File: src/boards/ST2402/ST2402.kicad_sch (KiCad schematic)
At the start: 21 parts, among them J1 Conn_02x19_Odd_Even, J2 Conn_02x19_Odd_Even, J3 Conn_01x08, J4 Conn_01x08, J5 Conn_01x06, J6 Conn_01x10, J7 Conn_01x02, J8 Conn_01x02

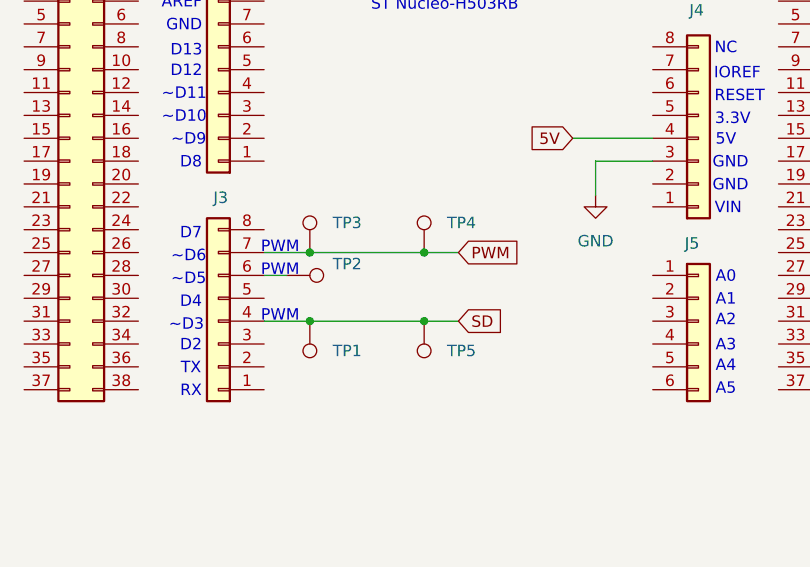
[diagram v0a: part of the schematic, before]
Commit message: Updated pcb files
Added r2 and r3 gerbers and updated KiCad file (r3)
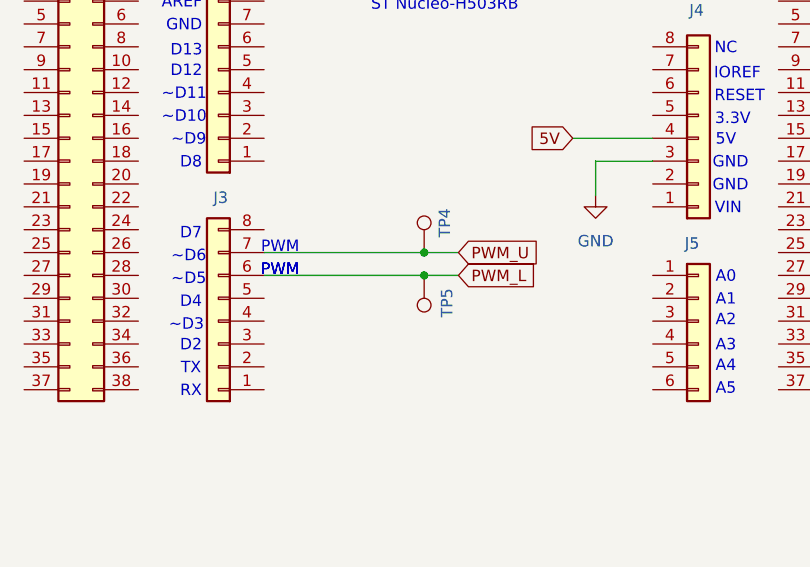
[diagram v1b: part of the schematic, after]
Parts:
- removed TP1, TP2, TP3: TestPoint, TestPoint:TestPoint_THTPad_D2.0mm_Drill1.0mm, symbol Connector:TestPoint
- TP4, TP5: footprint TestPoint:TestPoint_THTPad_D2.0mm_Drill1.0mm -> TestPoint:TestPoint_Keystone_5010-5014_Multipurpose
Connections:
- net PWM_L: now reaches J3.6 (Pin_6)
- net PWM_L: now also TP5.1
- net PWM renamed PWM_U
- net SD: no longer names the net of J3.4 (Pin_4)
- net SD: no longer TP5.1
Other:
- moved on the sheet: TP5
